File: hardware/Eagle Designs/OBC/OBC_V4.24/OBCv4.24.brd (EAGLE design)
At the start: 90.2 x 95.5 mm, 38 parts, among them J1 MCX-J-P-H-RA-TH1, J10 5037630591, J11 5037630291, J12 5037630491, J13 5037630291, J14 5037630491, J2 5037630491, J3 5037630591, J4 5037630291, J5 5037630291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

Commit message: OBC V4.24
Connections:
- removed net PI_STATUS: U$1.32-OUT1B, X1.8
- new net UART6_RX: U$1.7-RX2/OUT1A, X1.8
- new net UART6_TX: U$1.8-TX2/IN1, X1.10
- net NIRQ: now also U$1.40-A16/CS1; no longer U$1.8-TX2/IN1
- net RADIO_RESET: now also U$1.32-OUT1B; no longer U$1.7-RX2/OUT1A
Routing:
- net PI_STATUS: track 88.3 -> 0.00 mm
- net UART6_RX: track 0.00 -> 60.3 mm, vias 0 -> 1
- net UART6_TX: track 0.00 -> 59.0 mm, vias 0 -> 1
- net RADIO_RESET: track 87.6 -> 130.7 mm
- net NIRQ: track 86.8 -> 90.8 mm
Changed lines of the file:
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@@
 </signal>
 <signal name="RADIO_RESET">
-<contactref element="U$1" pad="7-RX2/OUT1A"/>
 <contactref element="U4" pad="6"/>
 <via x="41.76" y="25.88" extent="1-16" drill="0.35"/>
@@
 <wire x1="41.76" y1="25.88" x2="37.87" y2="21.99" width="0.6" layer="2"/>
 <wire x1="37.87" y1="21.99" x2="32.07" y2="21.99" width="0.6" layer="2"/>
-<wire x1="41.1" y1="56.46" x2="36.36" y2="61.2" width="0.4" layer="16"/>
-<wire x1="36.36" y1="64.11" x2="36.36" y2="61.2" width="0.4" layer="16"/>
-<wire x1="41.1" y1="56.46" x2="41.1" y2="46.01" width="0.4" layer="16"/>
 <contactref element="U3" pad="14"/>
 <wire x1="32.67" y1="19.1" x2="35.65" y2="19.1" width="0.5" layer="16"/>
@@
 <wire x1="35.65" y1="19.1" x2="41.44908125" y2="19.1" width="0.5" layer="16"/>
 <wire x1="41.44908125" y1="19.1" x2="41.76" y2="19.41091875" width="0.5" layer="16"/>
-<wire x1="48.32" y1="38.79" x2="48.32" y2="35.57" width="0.4" layer="16"/>
-<wire x1="41.1" y1="46.01" x2="48.32" y2="38.79" width="0.4" layer="16"/>
-<wire x1="41.76" y1="25.88" x2="42.97" y2="25.88" width="0.4" layer="16"/>
-<wire x1="42.97" y1="25.88" x2="44.82" y2="27.73" width="0.4" layer="16"/>
-<wire x1="44.82" y1="27.73" x2="46.17" y2="27.73" width="0.4" layer="16"/>
-<wire x1="48.38" y1="29.94" x2="46.17" y2="27.73" width="0.4" layer="16"/>
-<wire x1="48.3" y1="35.59" x2="48.32" y2="35.57" width="0.3" layer="16"/>
-<wire x1="48.32" y1="35.57" x2="48.38" y2="35.51" width="0.3" layer="16"/>
-<wire x1="48.38" y1="35.51" x2="48.38" y2="29.94" width="0.3" layer="16"/>
+<contactref element="U$1" pad="32-OUT1B"/>
+<wire x1="41.76" y1="25.88" x2="44.87" y2="22.77" width="0.508" layer="1"/>
+<wire x1="44.87" y1="22.77" x2="67.97" y2="22.77" width="0.508" layer="1"/>
+<wire x1="67.97" y1="22.77" x2="81.31" y2="36.11" width="0.508" layer="1"/>
+<wire x1="81.31" y1="36.11" x2="84.74" y2="36.11" width="0.508" layer="1"/>
+<wire x1="84.74" y1="36.11" x2="86.96" y2="38.33" width="0.508" layer="1"/>
+<wire x1="86.96" y1="38.33" x2="86.96" y2="63" width="0.508" layer="1"/>
+<wire x1="86.96" y1="63" x2="85.81" y2="64.15" width="0.508" layer="1"/>
+<wire x1="85.81" y1="64.15" x2="74.5" y2="64.15" width="0.508" layer="1"/>
+<wire x1="74.5" y1="64.15" x2="74.46" y2="64.11" width="0.508" layer="1"/>
 </signal>
 <signal name="3V3_BUS">
@@
 <wire x1="35.65" y1="21.1" x2="35.44" y2="21.1" width="0.6" layer="16"/>
 </signal>
-<signal name="PI_STATUS">
-<contactref element="U$1" pad="32-OUT1B"/>
-<contactref element="X1" pad="8"/>
-<wire x1="26.78" y1="35.814" x2="26.78" y2="37.33" width="0.5" layer="1"/>
-<wire x1="26.78" y1="37.33" x2="27.9" y2="38.45" width="0.5" layer="1"/>
-<wire x1="27.9" y1="38.45" x2="34.35" y2="38.45" width="0.5" layer="1"/>
-<wire x1="84.75" y1="52.66" x2="86.37" y2="54.28" width="0.5" layer="1"/>
-<wire x1="86.37" y1="54.28" x2="86.37" y2="61.41" width="0.5" layer="1"/>
-<wire x1="83.67" y1="64.11" x2="74.46" y2="64.11" width="0.5" layer="1"/>
-<wire x1="34.35" y1="38.45" x2="48.56" y2="52.66" width="0.5" layer="1"/>
-<wire x1="48.56" y1="52.66" x2="84.75" y2="52.66" width="0.5" layer="1"/>
-<wire x1="86.37" y1="61.41" x2="83.67" y2="64.11" width="0.5" layer="1"/>
-</signal>
 <signal name="NIRQ">
 <contactref element="U3" pad="6"/>
-<contactref element="U$1" pad="8-TX2/IN1"/>
 <via x="77.86" y="13.87" extent="1-16" drill="0.35"/>
 <wire x1="77.86" y1="13.87" x2="77.69" y2="14.04" width="0.6" layer="16"/>
@@
 <wire x1="77.86" y1="13.87" x2="79.48" y2="15.49" width="0.7" layer="15"/>
 <wire x1="79.48" y1="15.49" x2="79.48" y2="34.63" width="0.7" layer="15"/>
-<wire x1="62.54" y1="40.47" x2="38.9" y2="64.11" width="0.7" layer="2"/>
-<via x="64.66" y="40.53" extent="1-16" drill="0.35"/>
-<wire x1="64.66" y1="40.53" x2="64.6" y2="40.47" width="0.7" layer="2"/>
-<wire x1="64.6" y1="40.47" x2="62.54" y2="40.47" width="0.7" layer="2"/>
-<wire x1="73.58" y1="40.53" x2="64.66" y2="40.53" width="0.7" layer="15"/>
 <wire x1="79.48" y1="34.63" x2="73.58" y2="40.53" width="0.7" layer="15"/>
+<contactref element="U$1" pad="40-A16/CS1"/>
+<wire x1="73.58" y1="40.53" x2="73.25" y2="40.86" width="0.8128" layer="15"/>
+<wire x1="73.25" y1="62.76" x2="73.25" y2="40.86" width="0.8128" layer="15"/>
+<wire x1="61.2583" y1="73.0588" x2="56.68" y2="77.6371" width="0.6096" layer="1"/>
+<wire x1="56.68" y1="77.6371" x2="56.68" y2="79.35" width="0.6096" layer="1"/>
+<wire x1="61.2583" y1="73.0588" x2="62.9712" y2="73.0588" width="0.6096" layer="1"/>
+<via x="65.84" y="73.05" extent="1-16" drill="0.35"/>
+<wire x1="62.9712" y1="73.0588" x2="65.8312" y2="73.0588" width="0.508" layer="1"/>
+<wire x1="65.8312" y1="73.0588" x2="65.84" y2="73.05" width="0.508" layer="1"/>
+<wire x1="65.84" y1="73.05" x2="73.2488" y2="65.6412" width="0.508" layer="15"/>
+<wire x1="73.2488" y1="62.7612" x2="73.25" y2="62.76" width="0.508" layer="15"/>
+<wire x1="73.2488" y1="65.6412" x2="73.2488" y2="62.7612" width="0.508" layer="15"/>
 </signal>
 <signal name="RX_ON">
@@
 <contactref element="U$1" pad="+5V"/>
 </signal>
+<signal name="UART6_RX">
+<contactref element="U$1" pad="7-RX2/OUT1A"/>
+<contactref element="X1" pad="8"/>
+<wire x1="26.78" y1="35.814" x2="26.78" y2="37.33" width="0.5" layer="1"/>
+<wire x1="26.78" y1="37.33" x2="27.9" y2="38.45" width="0.5" layer="1"/>
+<wire x1="27.9" y1="38.45" x2="34.35" y2="38.45" width="0.5" layer="1"/>
+<wire x1="45.0646" y1="53.1560375" x2="45.24" y2="53.3314375" width="0.6096" layer="1"/>
+<wire x1="34.35" y1="38.45" x2="45.0646" y2="49.1646" width="0.6096" layer="1"/>
+<wire x1="45.0646" y1="49.1646" x2="45.0646" y2="53.1560375" width="0.6096" layer="1"/>
+<via x="44.37" y="72.58" extent="1-16" drill="0.35"/>
+<wire x1="45.24" y1="71.71" x2="44.37" y2="72.58" width="0.6096" layer="1"/>
+<wire x1="45.24" y1="53.3314375" x2="45.24" y2="71.71" width="0.6096" layer="1"/>
+<wire x1="44.37" y1="72.58" x2="44.37" y2="72.12" width="0.6096" layer="15"/>
+<wire x1="44.37" y1="72.12" x2="36.36" y2="64.11" width="0.6096" layer="15"/>
+</signal>
+<signal name="UART6_TX">
+<contactref element="U$1" pad="8-TX2/IN1"/>
+<contactref element="X1" pad="10"/>
+<wire x1="50.24" y1="67.8" x2="50.24" y2="67.92" width="0.508" layer="1"/>
+<via x="47.19" y="70.57" extent="1-16" drill="0.35"/>
+<wire x1="50.24" y1="67.8" x2="47.47" y2="70.57" width="0.508" layer="1"/>
+<wire x1="47.47" y1="70.57" x2="47.19" y2="70.57" width="0.508" layer="1"/>
+<wire x1="47.19" y1="70.57" x2="43.02" y2="66.4" width="0.508" layer="15"/>
+<wire x1="41.19" y1="66.4" x2="38.9" y2="64.11" width="0.508" layer="15"/>
+<wire x1="43.02" y1="66.4" x2="41.19" y2="66.4" width="0.508" layer="15"/>
+<wire x1="50.24" y1="51.63" x2="36.31" y2="37.7" width="0.508" layer="1"/>
+<wire x1="36.2712" y1="37.7388" x2="36.31" y2="37.7" width="0.508" layer="1"/>
+<wire x1="50.24" y1="67.8" x2="50.24" y2="51.63" width="0.508" layer="1"/>
+<wire x1="36.31" y1="37.7" x2="35.86" y2="37.25" width="0.508" layer="1"/>
+<wire x1="30.756" y1="37.25" x2="29.32" y2="35.814" width="0.508" layer="1"/>
+<wire x1="35.86" y1="37.25" x2="30.756" y2="37.25" width="0.508" layer="1"/>
+</signal>
 </signals>

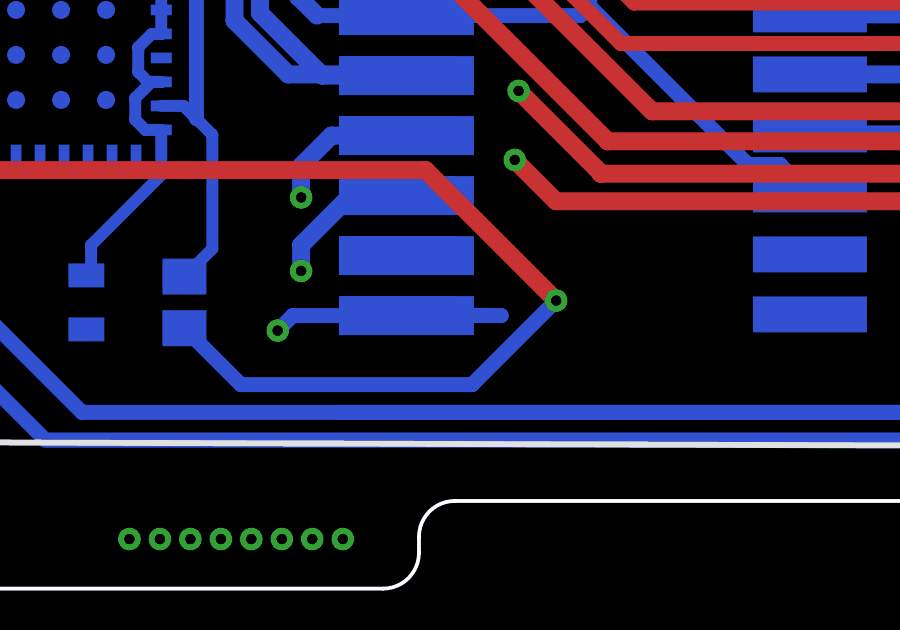
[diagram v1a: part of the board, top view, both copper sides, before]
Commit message: cleaned up a wire stub on OBC 4.24 and copied OBC for RF with ground plane
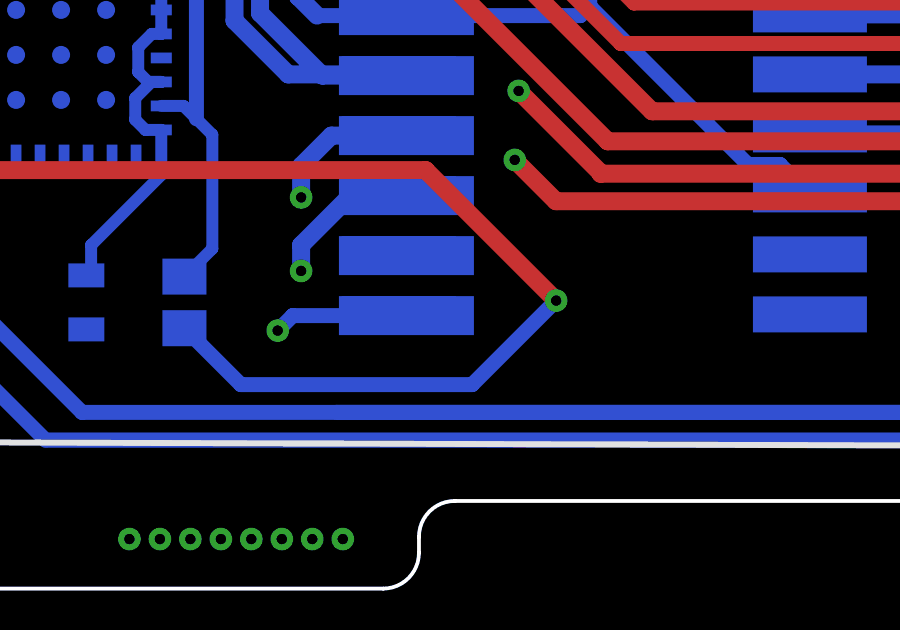
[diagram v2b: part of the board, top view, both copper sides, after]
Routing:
- net ANT_CONN: track 114.6 -> 108.1 mm
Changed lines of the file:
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@@
 <wire x1="78.27" y1="5.32" x2="34.64" y2="5.32" width="0.8" layer="15"/>
 <wire x1="31.36" y1="8.6" x2="34.64" y2="5.32" width="0.8" layer="15"/>
-<wire x1="35.65" y1="9.1" x2="38.805" y2="9.1" width="0.5" layer="16"/>
-<wire x1="35.4" y1="9.14" x2="38.805" y2="9.1" width="0.5" layer="16"/>
+<wire x1="35.65" y1="9.1" x2="35.4" y2="9.14" width="0" layer="19" extent="16-16"/>
 </signal>
 <signal name="N$16">

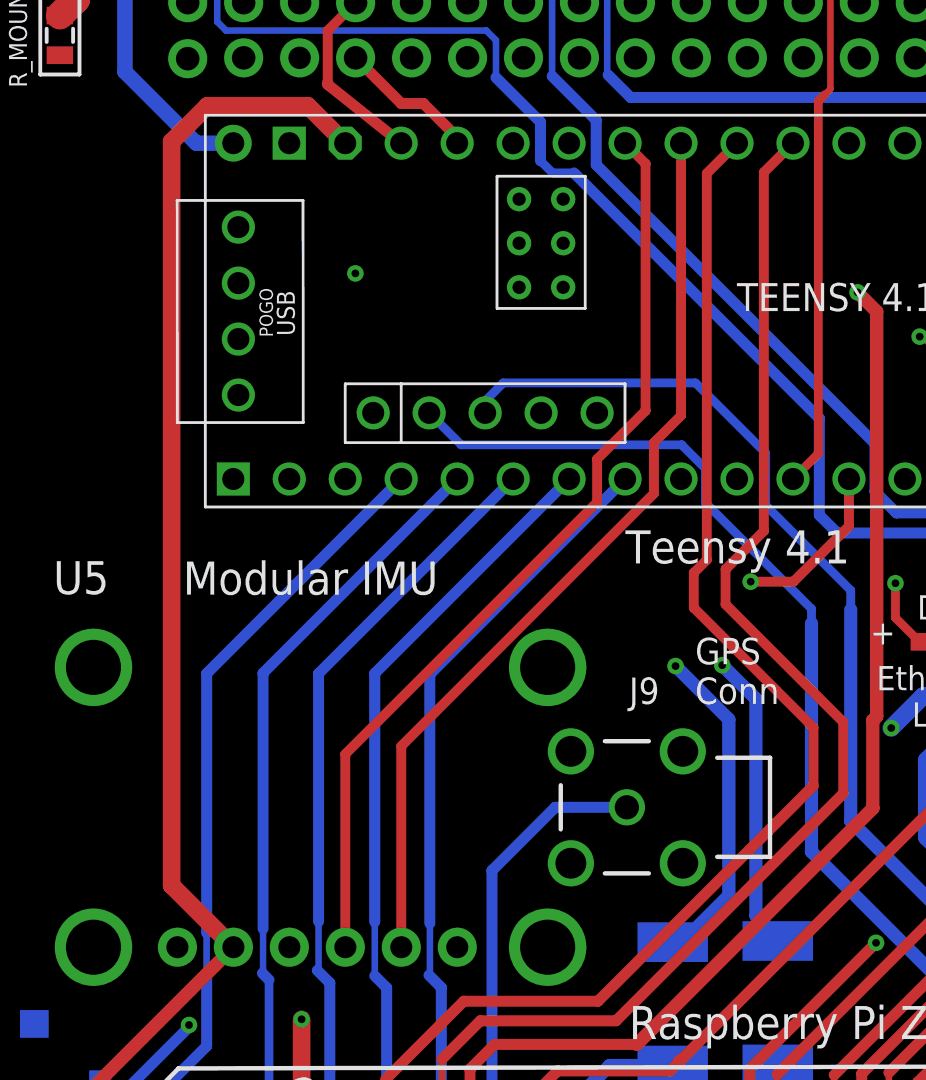
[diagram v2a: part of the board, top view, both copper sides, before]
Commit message: changed radio power supply from 5V_bus to SW_3V3_2 on both the OBCv2.24 and OBCv2.24_RFplane. Added ground station board.
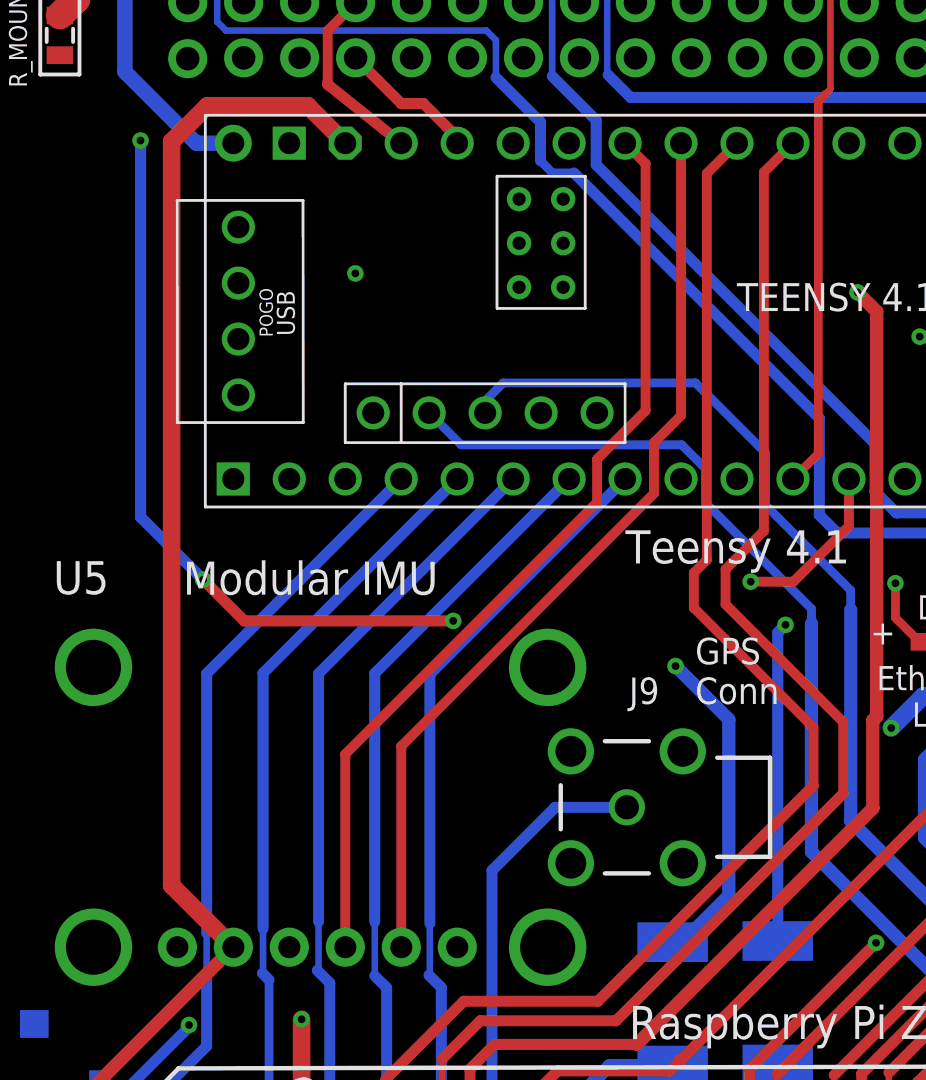
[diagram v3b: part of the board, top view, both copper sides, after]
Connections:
- new net SW_3V3_2: H1.2.20, R8.2
- net 5V_BUS: no longer R8.2
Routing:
- net SW_3V3_2: track 0.00 -> 98.0 mm, vias 0 -> 4
- net 5V_BUS: track 150.4 -> 128.0 mm, vias 3 -> 2
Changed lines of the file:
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@@
 <wire x1="23.78" y1="61.98" x2="38.63" y2="61.98" width="0.7" layer="2"/>
 <wire x1="22.39" y1="63.37" x2="23.78" y2="61.98" width="0.7" layer="2"/>
-<via x="38.23" y="55.66" extent="1-16" drill="0.35"/>
-<wire x1="39.76" y1="54.13" x2="39.76" y2="44.29" width="0.6" layer="16"/>
-<wire x1="39.76" y1="54.13" x2="38.23" y2="55.66" width="0.6" layer="16"/>
-<wire x1="38.23" y1="55.66" x2="43.05" y2="55.66" width="0.8" layer="2"/>
-<wire x1="43.05" y1="55.66" x2="45.9" y2="52.81" width="0.8" layer="2"/>
-<contactref element="R8" pad="2"/>
-<wire x1="39.76" y1="44.29" x2="40.75" y2="43.3" width="0.6" layer="16"/>
-<wire x1="40.75" y1="43.3" x2="40.75" y2="43.14" width="0.6" layer="16"/>
 <via x="21.58" y="73.44" extent="1-16" drill="0.35"/>
 <wire x1="21.58" y1="73.44" x2="21.58" y2="70.94084375" width="0.6096" layer="2"/>
@@
 <wire x1="35.86" y1="37.25" x2="30.756" y2="37.25" width="0.508" layer="1"/>
 </signal>
+<signal name="SW_3V3_2">
+<contactref element="H1" pad="2.20"/>
+<contactref element="R8" pad="2"/>
+<via x="41.1" y="57.49" extent="1-16" drill="0.35"/>
+<via x="26.02" y="57.67" extent="1-16" drill="0.35"/>
+<via x="14.67" y="59.54" extent="1-16" drill="0.35"/>
+<via x="11.83" y="79.47" extent="1-16" drill="0.35"/>
+<wire x1="40.75" y1="43.14" x2="40.75" y2="57.14" width="0.508" layer="16"/>
+<wire x1="40.75" y1="57.14" x2="41.1" y2="57.49" width="0.508" layer="16"/>
+<wire x1="41.1" y1="57.49" x2="40.37" y2="58.22" width="0.508" layer="2"/>
+<wire x1="26.57" y1="58.22" x2="26.02" y2="57.67" width="0.508" layer="2"/>
+<wire x1="40.37" y1="58.22" x2="26.57" y2="58.22" width="0.508" layer="2"/>
+<wire x1="26.02" y1="57.67" x2="16.54" y2="57.67" width="0.508" layer="1"/>
+<wire x1="16.54" y1="57.67" x2="14.67" y2="59.54" width="0.508" layer="1"/>
+<wire x1="14.67" y1="59.54" x2="11.83" y2="62.38" width="0.508" layer="16"/>
+<wire x1="11.83" y1="62.38" x2="11.83" y2="79.47" width="0.508" layer="16"/>
+<wire x1="11.83" y1="79.47" x2="11.83" y2="85.78" width="0.508" layer="2"/>
+<wire x1="13.1085" y1="87.0585" x2="34.78975" y2="87.0585" width="0.508" layer="2"/>
+<wire x1="35.59" y1="87.85875" x2="35.59" y2="89.97" width="0.508" layer="2"/>
+<wire x1="35.59" y1="89.97" x2="36.425" y2="90.805" width="0.508" layer="2"/>
+<wire x1="36.425" y1="90.805" x2="36.83" y2="90.805" width="0.508" layer="2"/>
+<wire x1="11.83" y1="85.78" x2="13.1085" y2="87.0585" width="0.508" layer="2"/>
+<wire x1="34.78975" y1="87.0585" x2="35.59" y2="87.85875" width="0.508" layer="2"/>
+</signal>
 </signals>
